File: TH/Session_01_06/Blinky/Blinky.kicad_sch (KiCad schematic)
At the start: 12 parts

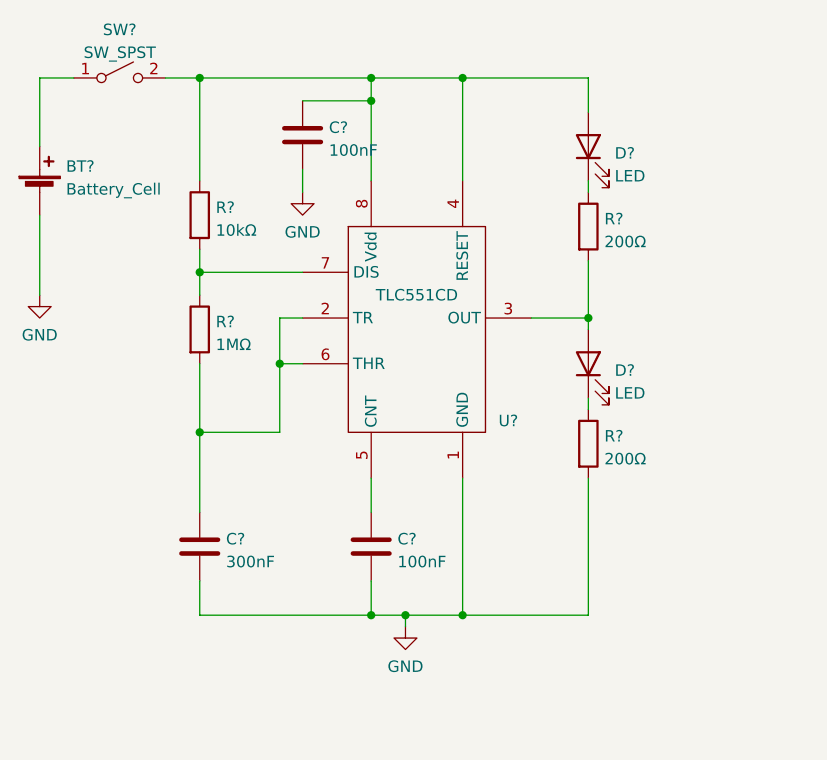
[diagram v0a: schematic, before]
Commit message: Revamps the through-hole project as transistor based
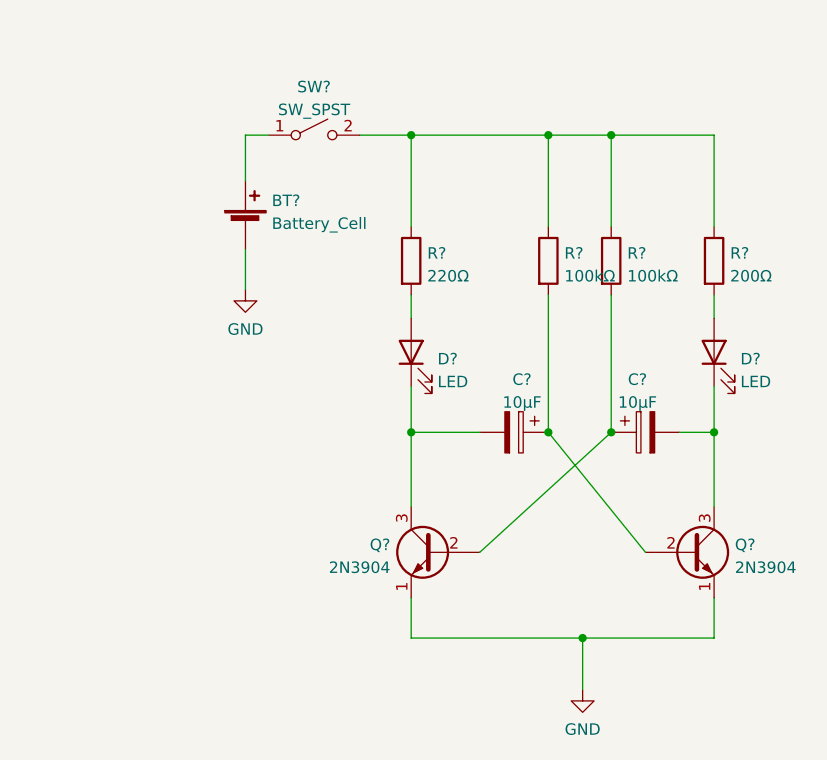
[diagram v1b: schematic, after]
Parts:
- removed BT?: Battery_Cell, symbol Device:Battery_Cell
- removed C? (x2): 100nF, symbol Device:C
- removed C?: 300nF, symbol Device:C
- removed D? (x2): LED, symbol Device:LED
- removed R? (x2): 200Ω, symbol Device:R
- removed R?: 10kΩ, symbol Device:R
- removed R?: 1MΩ, symbol Device:R
- removed SW?: SW_SPST, symbol Switch:SW_SPST
- removed U?: TLC551CD‎, Package_SO:SOIC-8_3.9x4.9mm_P1.27mm, symbol Blinky:TLC551CD‎
- added BT?: Battery_Cell, symbol Device:Battery_Cell
- added C? (x2): 10μF, symbol Device:C_Polarized
- added D? (x2): LED, symbol Device:LED
- added Q? (x2): 2N3904, Package_TO_SOT_THT:TO-92_Inline, symbol Transistor_BJT:2N3904
- added R? (x2): 100kΩ, symbol Device:R
- added R?: 220Ω, symbol Device:R
- added R?: 200Ω, symbol Device:R
- added SW?: SW_SPST, symbol Switch:SW_SPST
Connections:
- net GND: now also BT?.2 (-), Q?.1 (E), Q?.1 (E)
- new net: C?.2, D?.1 (K), Q?.3 (C) (x2)
- new net: D?.2 (A), R?.2 (x2)
- new net: R?.1, R?.1, R?.1, R?.1, SW?.2 (B)
- new net: C?.1, Q?.2 (B), R?.2 (x2)
- new net: BT?.1 (+), SW?.1 (A)
